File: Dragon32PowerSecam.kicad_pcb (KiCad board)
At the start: 2 copper layers, 246 x 83.9 mm, 24 parts, among them IC1 MC3346, IC2 MC3346, IC3 MC3346

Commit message: video tracing
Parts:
- added R10: 220R, Dragon:R_Axial_DIN0309_L9.0mm_D2.5mm_P12.70mm_Horizontal, F.Cu at (82.4, 50.8)
- added R12: 220R, Dragon:R_Axial_DIN0309_L9.0mm_D2.5mm_P12.70mm_Horizontal, F.Cu at (82.4, 55.9)
- added R14: 220R, Dragon:R_Axial_DIN0309_L9.0mm_D2.5mm_P12.70mm_Horizontal, F.Cu at (82.4, 48.3)
- added R40: 500R, Dragon:R_Axial_DIN0309_L9.0mm_D2.5mm_P12.70mm_Horizontal, F.Cu at (67.4, 60.9)
- added R47: 2R2, Dragon:R_Axial_DIN0309_L9.0mm_D2.5mm_P12.70mm_Horizontal, F.Cu at (58.0, 34.5)
- added R48: 2R2, Dragon:R_Axial_DIN0309_L9.0mm_D2.5mm_P12.70mm_Horizontal, F.Cu at (58.0, 32.0)
- added R8: 220R, Dragon:R_Axial_DIN0309_L9.0mm_D2.5mm_P12.70mm_Horizontal, F.Cu at (82.4, 53.4)
- added T1: Q_NPN_CBE, Package_TO_SOT_THT:TO-92, F.Cu at (94.8, 61.3)
- added T2: Q_NPN_CBE, Package_TO_SOT_THT:TO-92, F.Cu at (99.6, 61.3)
- added T3: Q_NPN_CBE, Package_TO_SOT_THT:TO-92, F.Cu at (90.1, 61.3)
- added T4: Q_NPN_CBE, Package_TO_SOT_THT:TO-92, F.Cu at (104.3, 61.3)
- added UM1: ~, Dragon:RF_Modulator_Astec_UM1601, F.Cu at (46.9, 71.9)
- moved C13 4.66 mm to (54.2, 29.4)
- moved R36 2.35 mm to (58.0, 29.5)
- moved C14 2.19 mm to (78.2, 53.5)
- moved C19 2.17 mm to (68.9, 42.4)
- moved C16 1.99 mm to (67.4, 79.8)
- moved IC2 1.79 mm to (84.9, 64.4)
- moved IC3 1.70 mm to (69.9, 64.4)
- moved C17 1.70 mm to (69.9, 83.2)
- moved C15 1.70 mm to (80.0, 72.0)
- moved L1 1.10 mm to (71.1, 52.2)
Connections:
- C14 pad 1: unconnected-(C14-Pad1) -> /Video/ic3_11
- C14 pad 2: unconnected-(C14-Pad2) -> /Video/ic3_8
- C15 pad 2: unconnected-(C15-Pad2) -> /Video/ic3_11
- C17 pad 1: unconnected-(C17-Pad1) -> /Video/ic3_4
- C19 pad 1: unconnected-(C19-Pad1) -> /Video/ic3_4
- C19 pad 2: unconnected-(C19-Pad2) -> Net-(C19-Pad2)
- IC3 pad 11: unconnected-(IC3-Pad11) -> /Video/ic3_11
- IC3 pad 14: unconnected-(IC3-Pad14) -> Net-(IC3-Pad14)
- IC3 pad 2: unconnected-(IC3-Pad2) -> Net-(IC3-Pad2)
- IC3 pad 3: unconnected-(IC3-Pad3) -> Net-(IC3-Pad14)
- IC3 pad 4: unconnected-(IC3-Pad4) -> /Video/ic3_4
- IC3 pad 5: unconnected-(IC3-Pad5) -> /Video/ic3_5
- IC3 pad 8: unconnected-(IC3-Pad8) -> /Video/ic3_8
- IC3 pad 9: unconnected-(IC3-Pad9) -> Net-(IC3-Pad2)
- L1 pad 1: unconnected-(L1-Pad1) -> /Video/ic3_8
- L1 pad 3: unconnected-(L1-Pad3) -> /Video/ic3_11
- L1 pad 5: unconnected-(L1-GND-Pad5) -> GND
- PL11 pad 4: unconnected-(PL11-Pad4) -> pl11_4
- PL11 pad 5: unconnected-(PL11-Pad5) -> pl11_5
- PL11 pad 6: unconnected-(PL11-Pad6) -> pl11_6
- PL11 pad 7: unconnected-(PL11-Pad7) -> pl11_7
- R39 pad 2: unconnected-(R39-Pad2) -> Net-(UM1-Bias)
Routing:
- net GND: track 4.93 -> 94.8 mm, vias 0 -> 4
- net /Video/ic3_5: track 0.00 -> 74.6 mm
- net /Video/ic3_4: track 0.00 -> 54.9 mm
- net /Video/ic3_8: track 0.00 -> 53.1 mm
- net unconnected-(IC3-Pad13): track 0.00 -> 36.2 mm
- net unconnected-(IC3-Pad12): track 0.00 -> 31.5 mm
- net Net-(IC3-Pad2): track 0.00 -> 28.1 mm
- net /Video/ic3_11: track 0.00 -> 26.1 mm, vias 0 -> 1
- net unconnected-(R48-Pad2): track 0.00 -> 23.8 mm
- net pl11_7: track 0.00 -> 16.5 mm
- net pl11_4: track 0.00 -> 13.8 mm
- net Net-(C19-Pad2): track 0.00 -> 13.1 mm
- net Net-(IC3-Pad14): track 0.00 -> 9.72 mm
- net pl11_6: track 0.00 -> 9.39 mm
- net pl11_5: track 0.00 -> 9.36 mm
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
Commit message: more video tracing
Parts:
- added C1: 1M250, Capacitor_THT:C_Rect_L16.5mm_W5.0mm_P15.00mm_MKT, F.Cu at (121.3, 97.3)
- added C2: 100nF, Capacitor_THT:C_Disc_D4.3mm_W1.9mm_P5.00mm, F.Cu at (123.1, 78.1)
- added D9: 1N, Diode_THT:D_A-405_P12.70mm_Horizontal, F.Cu at (117.7, 94.8)
- added R11: 220R, Dragon:R_Axial_DIN0309_L9.0mm_D2.5mm_P12.70mm_Horizontal, F.Cu at (97.2, 72.0)
- added R13: 220R, Dragon:R_Axial_DIN0309_L9.0mm_D2.5mm_P12.70mm_Horizontal, F.Cu at (97.2, 64.4)
- added R15: 220R, Dragon:R_Axial_DIN0309_L9.0mm_D2.5mm_P12.70mm_Horizontal, F.Cu at (97.2, 74.5)
- added R16: 220R, Dragon:R_Axial_DIN0309_L9.0mm_D2.5mm_P12.70mm_Horizontal, F.Cu at (82.5, 85.9)
- added R17: 220R, Dragon:R_Axial_DIN0309_L9.0mm_D2.5mm_P12.70mm_Horizontal, F.Cu at (112.2, 94.7)
- added R18: 220R, Resistor_THT:R_Axial_DIN0207_L6.3mm_D2.5mm_P10.16mm_Horizontal, F.Cu at (117.2, 79.6)
- added R19: 220R, Dragon:R_Axial_DIN0309_L9.0mm_D2.5mm_P12.70mm_Horizontal, F.Cu at (109.7, 94.7)
- added R20: 220R, Resistor_THT:R_Axial_DIN0207_L6.3mm_D2.5mm_P10.16mm_Horizontal, F.Cu at (119.7, 79.6)
- added R21: 220R, Dragon:R_Axial_DIN0309_L9.0mm_D2.5mm_P12.70mm_Horizontal, F.Cu at (114.8, 94.7)
- added R22: 220R, Dragon:R_Axial_DIN0309_L9.0mm_D2.5mm_P12.70mm_Horizontal, F.Cu at (94.9, 66.9)
- added R23: 220R, Dragon:R_Axial_DIN0309_L9.0mm_D2.5mm_P12.70mm_Horizontal, F.Cu at (97.7, 51.9)
- added R24: 220R, Dragon:R_Axial_DIN0309_L9.0mm_D2.5mm_P12.70mm_Horizontal, F.Cu at (82.5, 88.5)
- added R25: 220R, Dragon:R_Axial_DIN0309_L9.0mm_D2.5mm_P12.70mm_Horizontal, F.Cu at (97.7, 46.9)
- added R26: 220R, Dragon:R_Axial_DIN0309_L9.0mm_D2.5mm_P12.70mm_Horizontal, F.Cu at (82.5, 91.0)
- added R27: 220R, Dragon:R_Axial_DIN0309_L9.0mm_D2.5mm_P12.70mm_Horizontal, F.Cu at (97.7, 49.4)
- added R28: 220R, Dragon:R_Axial_DIN0309_L9.0mm_D2.5mm_P12.70mm_Horizontal, F.Cu at (97.7, 54.5)
- added R29: 220R, Dragon:R_Axial_DIN0309_L9.0mm_D2.5mm_P12.70mm_Horizontal, F.Cu at (82.5, 96.1)
- added R30: 220R, Dragon:R_Axial_DIN0309_L9.0mm_D2.5mm_P12.70mm_Horizontal, F.Cu at (82.5, 93.5)
- added R31: 220R, Dragon:R_Axial_DIN0309_L9.0mm_D2.5mm_P12.70mm_Horizontal, F.Cu at (82.5, 101.2)
- added R32: 220R, Dragon:R_Axial_DIN0309_L9.0mm_D2.5mm_P12.70mm_Horizontal, F.Cu at (82.5, 98.6)
- added R33: 220R, Dragon:R_Axial_DIN0309_L9.0mm_D2.5mm_P12.70mm_Horizontal, F.Cu at (97.3, 96.1)
- added R34: 220R, Dragon:R_Axial_DIN0309_L9.0mm_D2.5mm_P12.70mm_Horizontal, F.Cu at (97.2, 79.6)
- added R35: 220R, Dragon:R_Axial_DIN0309_L9.0mm_D2.5mm_P12.70mm_Horizontal, F.Cu at (84.5, 103.7)
- added R37: 220R, Dragon:R_Axial_DIN0309_L9.0mm_D2.5mm_P12.70mm_Horizontal, F.Cu at (97.7, 41.8)
- added R38: 220R, Dragon:R_Axial_DIN0309_L9.0mm_D2.5mm_P12.70mm_Horizontal, F.Cu at (97.7, 39.2)
- added R41: 220R, Dragon:R_Axial_DIN0309_L9.0mm_D2.5mm_P12.70mm_Horizontal, F.Cu at (67.7, 88.5)
- added R42: 220R, Dragon:R_Axial_DIN0309_L9.0mm_D2.5mm_P12.70mm_Horizontal, F.Cu at (67.7, 91.0)
- added R43: 220R, Dragon:R_Axial_DIN0309_L9.0mm_D2.5mm_P12.70mm_Horizontal, F.Cu at (67.7, 96.1)
- added R44: 220R, Dragon:R_Axial_DIN0309_L9.0mm_D2.5mm_P12.70mm_Horizontal, F.Cu at (67.7, 93.5)
- added R45: 220R, Dragon:R_Axial_DIN0309_L9.0mm_D2.5mm_P12.70mm_Horizontal, F.Cu at (67.7, 85.9)
- added R46: 220R, Dragon:R_Axial_DIN0309_L9.0mm_D2.5mm_P12.70mm_Horizontal, F.Cu at (67.7, 98.6)
- added R49: 220R, Dragon:R_Axial_DIN0309_L9.0mm_D2.5mm_P12.70mm_Horizontal, F.Cu at (97.7, 44.3)
- added R50: 220R, Dragon:R_Axial_DIN0309_L9.0mm_D2.5mm_P12.70mm_Horizontal, F.Cu at (97.7, 36.7)
- added R6: 220R, Dragon:R_Axial_DIN0309_L9.0mm_D2.5mm_P12.70mm_Horizontal, F.Cu at (97.2, 77.1)
- added R7: 220R, Dragon:R_Axial_DIN0309_L9.0mm_D2.5mm_P12.70mm_Horizontal, F.Cu at (97.2, 69.5)
- added R9: 220R, Dragon:R_Axial_DIN0309_L9.0mm_D2.5mm_P12.70mm_Horizontal, F.Cu at (97.2, 66.9)
- C11: footprint Capacitor_THT:C_Disc_D4.3mm_W1.9mm_P5.00mm -> Capacitor_THT:C_Disc_D3.0mm_W2.0mm_P2.50mm
- PL9: value DE9_Plug_MountingHoles -> External Power
- T1, T2, T3, T4: footprint Package_TO_SOT_THT:TO-92 -> Package_TO_SOT_THT:TO-92_Wide
- moved C18 3.89 mm to (67.7, 101.1)
- moved C12 2.42 mm to (113.7, 74.6)
- moved C11 2.39 mm to (114.3, 79.6)
- moved T4 2.02 mm to (106.3, 61.8)
- moved IC1 2.00 mm to (99.4, 83.4)
- moved R10 1.42 mm to (82.5, 49.4)
- moved R12 1.42 mm to (82.5, 54.5)
- moved R14 1.42 mm to (82.5, 46.9)
- moved R8 1.42 mm to (82.5, 51.9)
- moved T2 1.25 mm to (100.7, 61.8)
- moved C10 0.77 mm to (109.8, 97.4)
- moved T3 0.70 mm to (89.6, 61.8)
- moved T1 0.61 mm to (95.1, 61.8)
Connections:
- C10 pad 2: unconnected-(C10-Pad2) -> GND
- C15 pad 1: unconnected-(C15-Pad1) -> Net-(C15-Pad1)
- C16 pad 1: unconnected-(C16-Pad1) -> Net-(C16-Pad1)
- C16 pad 2: unconnected-(C16-Pad2) -> Net-(C16-Pad2)
- C17 pad 2: unconnected-(C17-Pad2) -> /Video/ic3_2
- C18 pad 1: unconnected-(C18-Pad1) -> GND
- C18 pad 2: unconnected-(C18-Pad2) -> Net-(C18-Pad2)
- IC1 pad 1: unconnected-(IC1-Pad1) -> /Video/ic1_1
- IC1 pad 10: unconnected-(IC1-Pad10) -> /Video/ic1_10
- IC1 pad 12: unconnected-(IC1-Pad12) -> /Video/ic1_12
- IC1 pad 13: unconnected-(IC1-Pad13) -> /Video/ic1_13
- IC1 pad 14: unconnected-(IC1-Pad14) -> /Video/ic1_14
- IC1 pad 7: unconnected-(IC1-Pad7) -> /Video/ic1_7
- IC1 pad 8: unconnected-(IC1-Pad8) -> +5V
- IC2 pad 1: unconnected-(IC2-Pad1) -> /Video/ic2_1
- IC2 pad 10: unconnected-(IC2-Pad10) -> /Video/ic2_10
- IC2 pad 11: unconnected-(IC2-Pad11) -> /Video/ic2_11
- IC2 pad 12: unconnected-(IC2-Pad12) -> /Video/ic2_12
- IC2 pad 13: unconnected-(IC2-Pad13) -> /Video/ic2_13
- IC2 pad 14: unconnected-(IC2-Pad14) -> +5V
- IC2 pad 2: unconnected-(IC2-Pad2) -> /Video/ic2_6
- IC2 pad 3: unconnected-(IC2-Pad3) -> /Video/ic1_14
- IC2 pad 4: unconnected-(IC2-Pad4) -> /Video/ic2_6
- IC2 pad 5: unconnected-(IC2-Pad5) -> /Video/ic2_5
- IC2 pad 6: unconnected-(IC2-Pad6) -> /Video/ic2_6
- IC2 pad 7: unconnected-(IC2-Pad7) -> /Video/ic2_7
- IC2 pad 8: unconnected-(IC2-Pad8) -> /Video/ic2_8
- IC2 pad 9: unconnected-(IC2-Pad9) -> /Video/ic2_6
- IC3 pad 1: unconnected-(IC3-Pad1) -> /Video/ic3_8
- IC3 pad 10: unconnected-(IC3-Pad10) -> Net-(IC3-Pad10)
- IC3 pad 12: unconnected-(IC3-Pad12) -> Net-(C16-Pad2)
- IC3 pad 13: unconnected-(IC3-Pad13) -> Net-(IC3-Pad13)
- IC3 pad 2: Net-(IC3-Pad2) -> /Video/ic3_2
- IC3 pad 6: unconnected-(IC3-Pad6) -> Net-(C16-Pad1)
- IC3 pad 7: unconnected-(IC3-Pad7) -> Net-(IC3-Pad10)
- IC3 pad 9: Net-(IC3-Pad2) -> /Video/ic3_2
- PL11 pad 1: unconnected-(PL11-Pad1) -> pl11_1
- PL11 pad 2: unconnected-(PL11-Pad2) -> pl11_2
- PL11 pad 3: unconnected-(PL11-Pad3) -> pl11_3
- PL9 pad 1: unconnected-(PL9-Pad1) -> /Power/pl9_1
- PL9 pad 2: unconnected-(PL9-Pad2) -> /Power/pl9_2
- PL9 pad 3: unconnected-(PL9-Pad3) -> /Power/pl9_3
- PL9 pad 4: unconnected-(PL9-Pad4) -> GND
- PL9 pad 5: unconnected-(PL9-Pad5) -> /Power/pl9_5
- PL9 pad 6: unconnected-(PL9-Pad6) -> /Power/pl9_1
- PL9 pad 7: unconnected-(PL9-Pad7) -> /Power/pl9_2
- PL9 pad 8: unconnected-(PL9-Pad8) -> GND
- PL9 pad 9: unconnected-(PL9-Pad9) -> GND
- R10 pad 2: unconnected-(R10-Pad2) -> Net-(T2-E)
- R12 pad 2: unconnected-(R12-Pad2) -> Net-(T1-E)
- R14 pad 2: unconnected-(R14-Pad2) -> Net-(T4-E)
- R36 pad 2: unconnected-(R36-Pad2) -> +5V
- R40 pad 1: unconnected-(R40-Pad1) -> /Video/ic3_2
- R48 pad 2: unconnected-(R48-Pad2) -> SOUND
- R8 pad 2: unconnected-(R8-Pad2) -> Net-(T3-E)
- SW1 pad 11: unconnected-(SW1-B-Pad11) -> /Power/pl9_5
- SW1 pad 2: unconnected-(SW1-B-Pad2) -> /Power/pl9_1
- SW1 pad 5: (no net) -> /Power/pl9_2
- SW1 pad 8: unconnected-(SW1-B-Pad8) -> /Power/pl9_3
- T1 pad 1: unconnected-(T1-C-Pad1) -> +5V
- T1 pad 2: unconnected-(T1-B-Pad2) -> /Video/ic2_5
- T1 pad 3: unconnected-(T1-E-Pad3) -> Net-(T1-E)
- T2 pad 1: unconnected-(T2-C-Pad1) -> +5V
- T2 pad 2: unconnected-(T2-B-Pad2) -> /Video/ic2_11
- T2 pad 3: unconnected-(T2-E-Pad3) -> Net-(T2-E)
- T3 pad 1: unconnected-(T3-C-Pad1) -> +5V
- T3 pad 2: unconnected-(T3-B-Pad2) -> /Video/ic2_1
- T3 pad 3: unconnected-(T3-E-Pad3) -> Net-(T3-E)
- T4 pad 1: unconnected-(T4-C-Pad1) -> +5V
- T4 pad 2: unconnected-(T4-B-Pad2) -> /Video/ic2_8
- T4 pad 3: unconnected-(T4-E-Pad3) -> Net-(T4-E)
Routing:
- net +5V: track 0.00 -> 225.2 mm, vias 0 -> 1
- net SOUND: track 0.00 -> 114.4 mm, vias 0 -> 1
- net -5V: track 0.00 -> 108.1 mm
- net +12V: track 0.00 -> 89.1 mm
- net /Power/pl9_2: track 0.00 -> 57.3 mm
- net /Video/ic1_14: track 0.00 -> 56.3 mm, vias 0 -> 1
- net /Video/ic2_6: track 0.00 -> 55.7 mm
- net Net-(C16-Pad2): track 0.00 -> 55.0 mm
- net /Video/ic1_12: track 0.00 -> 53.0 mm
- net /Power/pl9_3: track 0.00 -> 52.9 mm
- net /Video/ic3_2: track 0.00 -> 52.0 mm
- net /Video/ic2_13: track 0.00 -> 45.0 mm
- net /Power/pl9_5: track 0.00 -> 40.8 mm
- net Net-(IC3-Pad13): track 0.00 -> 38.1 mm
- net /Power/pl9_1: track 0.00 -> 38.0 mm
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
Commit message: power tracing
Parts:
- added C5: 220uF 35V, Capacitor_THT:CP_Axial_L25.0mm_D10.0mm_P30.00mm_Horizontal, F.Cu at (150.0, 50.5)
- added C6: 4700uF 16V, Capacitor_THT:CP_Axial_L34.5mm_D20.0mm_P41.00mm_Horizontal, F.Cu at (211.3, 38.1)
- added C9: 4700uF 16V, Capacitor_THT:CP_Axial_L34.5mm_D20.0mm_P41.00mm_Horizontal, F.Cu at (218.5, 38.2)
- added D1: 1N5401, Diode_THT:D_DO-201AD_P15.24mm_Horizontal, F.Cu at (127.4, 50.7)
- added D2: 1N5401, Diode_THT:D_DO-201AD_P15.24mm_Horizontal, F.Cu at (127.4, 56.4)
- added D3: 1N4002, Diode_THT:D_DO-41_SOD81_P10.16mm_Horizontal, F.Cu at (133.0, 60.9)
- added D4: 1N4002, Diode_THT:D_DO-41_SOD81_P10.16mm_Horizontal, F.Cu at (133.0, 64.4)
- added D5: 1N5401, Diode_THT:D_DO-201AD_P15.24mm_Horizontal, F.Cu at (127.4, 68.9)
- added D6: 1N5401, Diode_THT:D_DO-201AD_P15.24mm_Horizontal, F.Cu at (127.5, 74.6)
- added D7: 1N4002, Diode_THT:D_DO-41_SOD81_P10.16mm_Horizontal, F.Cu at (133.0, 79.0)
- added D8: 1N4002, Diode_THT:D_DO-41_SOD81_P10.16mm_Horizontal, F.Cu at (133.0, 82.2)
- added R2: 220R, Dragon:R_Axial_DIN0309_L9.0mm_D2.5mm_P12.70mm_Horizontal, F.Cu at (125.3, 94.7)
- added R5: 180R, Resistor_THT:R_Axial_DIN0516_L15.5mm_D5.0mm_P20.32mm_Horizontal, F.Cu at (158.1, 75.0)
- added REG1: LM309K, Package_TO_SOT_THT:TO-3, F.Cu at (184.5, 68.5)
- moved C11 0.86 mm to (113.5, 79.6)
- moved C2 0.58 mm to (122.5, 78.1)
- moved C12 0.36 mm to (113.4, 74.6)
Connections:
- C1 pad 2: unconnected-(C1-Pad2) -> -5V
- C10 pad 1: unconnected-(C10-Pad1) -> LUMA
- C11 pad 1: unconnected-(C11-Pad1) -> Net-(C11-Pad1)
- C11 pad 2: unconnected-(C11-Pad2) -> /Video/ic1_3
- C12 pad 1: unconnected-(C12-Pad1) -> /Video/ic1_1
- C12 pad 2: unconnected-(C12-Pad2) -> /Video/ic2_12
- C2 pad 1: unconnected-(C2-Pad1) -> GND
- D9 pad 1: unconnected-(D9-K-Pad1) -> /Video/ic2_12
- D9 pad 2: unconnected-(D9-A-Pad2) -> Net-(D9-A)
- IC1 pad 11: unconnected-(IC1-Pad11) -> +5V
- IC1 pad 3: unconnected-(IC1-Pad3) -> /Video/ic1_3
- IC2 pad 2: /Video/ic2_6 -> GND
- IC2 pad 4: /Video/ic2_6 -> GND
- IC2 pad 6: /Video/ic2_6 -> GND
- IC2 pad 9: /Video/ic2_6 -> GND
- R17 pad 1: unconnected-(R17-Pad1) -> GND
- R17 pad 2: unconnected-(R17-Pad2) -> Net-(C11-Pad1)
- R18 pad 1: unconnected-(R18-Pad1) -> /Video/ic1_3
- R19 pad 1: unconnected-(R19-Pad1) -> GND
- R19 pad 2: unconnected-(R19-Pad2) -> /Video/ic1_3
- R20 pad 1: unconnected-(R20-Pad1) -> Net-(D9-A)
- R21 pad 1: unconnected-(R21-Pad1) -> GND
- R21 pad 2: unconnected-(R21-Pad2) -> Net-(D9-A)
- R35 pad 2: /Video/ic2_6 -> GND
- SW1 pad 10: unconnected-(SW1-A-Pad10) -> Net-(D4-K)
- SW1 pad 3: unconnected-(SW1-C-Pad3) -> Net-(D1-K)
- SW1 pad 6: unconnected-(SW1-C-Pad6) -> Net-(D2-K)
- SW1 pad 7: unconnected-(SW1-A-Pad7) -> Net-(D3-K)
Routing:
- net -5V: track 108.1 -> 280.6 mm
- net Net-(D7-K): track 0.00 -> 151.9 mm
- net /Power/VI: track 0.00 -> 127.6 mm
- net GND: track 123.8 -> 218.6 mm, vias 5 -> 6
- net +5V: track 225.2 -> 293.5 mm
- net /Video/ic2_6: track 55.7 -> 0.00 mm
- net Net-(D4-K): track 0.00 -> 53.6 mm, vias 0 -> 1
- net Net-(D3-K): track 0.00 -> 42.9 mm
- net Net-(D3-A): track 0.00 -> 42.4 mm
- net /Video/ic2_12: track 34.5 -> 75.5 mm, vias 1 -> 2
- net Net-(D2-K): track 0.00 -> 38.0 mm
- net Net-(D1-K): track 0.00 -> 33.7 mm
- net /Video/ic1_3: track 0.00 -> 26.4 mm
- net unconnected-(SW1-A-Pad7): track 19.4 -> 0.00 mm
- net unconnected-(SW1-C-Pad6): track 10.1 -> 0.00 mm
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- added copper zone on B.Cu, net /Power/VI

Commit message: layout and routing complete
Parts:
- added C3: 1M250, Capacitor_THT:C_Rect_L16.5mm_W5.0mm_P15.00mm_MKT, F.Cu at (146.7, 107.8)
- added C4: 1M250, Capacitor_THT:C_Rect_L16.5mm_W5.0mm_P15.00mm_MKT, F.Cu at (157.3, 107.7)
- added C7: 10nF, Capacitor_THT:C_Disc_D4.7mm_W2.5mm_P5.00mm, F.Cu at (257.7, 51.6)
- added C8: 470uF 50V, Capacitor_THT:CP_Axial_L30.0mm_D10.0mm_P35.00mm_Horizontal, F.Cu at (267.6, 86.7)
- added R3: 220R, Dragon:R_Axial_DIN0309_L9.0mm_D2.5mm_P12.70mm_Horizontal, F.Cu at (150.7, 92.8)
- added R4: 220R, Dragon:R_Axial_DIN0309_L9.0mm_D2.5mm_P12.70mm_Horizontal, F.Cu at (153.3, 92.8)
- added REG2: L7905, Package_TO_SOT_THT:TO-220-3_Vertical, F.Cu at (257.2, 67.7)
- added REG3: LM7812_TO220, Package_TO_SOT_THT:TO-220-3_Vertical, F.Cu at (257.2, 88.6)
- C12, C19: value C_Polarized_Small -> 1uF 25V Tant
- C13: value C_Polarized_Small -> 1uF 25V
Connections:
- C13 pad 1: Net-(UM1-Audio) -> /Video/ic3_8
- C13 pad 2: unconnected-(C13-Pad2) -> GND
- C2 pad 2: unconnected-(C2-Pad2) -> /Power/VI
- R2 pad 1: unconnected-(R2-Pad1) -> GND
- R36 pad 1: Net-(UM1-Audio) -> /Video/ic3_8
- R5 pad 1: unconnected-(R5-Pad1) -> Net-(REG2-VI)
- UM1 pad 3: Net-(UM1-Audio) -> /Video/ic3_8
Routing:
- net +12V: track 89.1 -> 251.3 mm
- net Net-(REG2-VI): track 0.00 -> 127.8 mm
- net /Video/ic3_8: track 64.8 -> 96.3 mm
- net Net-(UM1-Audio): track 16.7 -> 0.00 mm
- net GND: track 218.6 -> 234.6 mm
- net -5V: track 280.6 -> 271.7 mm
- net Net-(D7-K): track 151.9 -> 157.6 mm
- net /Power/VI: track 127.6 -> 131.6 mm
- net /Power/pl9_2: track 57.0 -> 56.5 mm

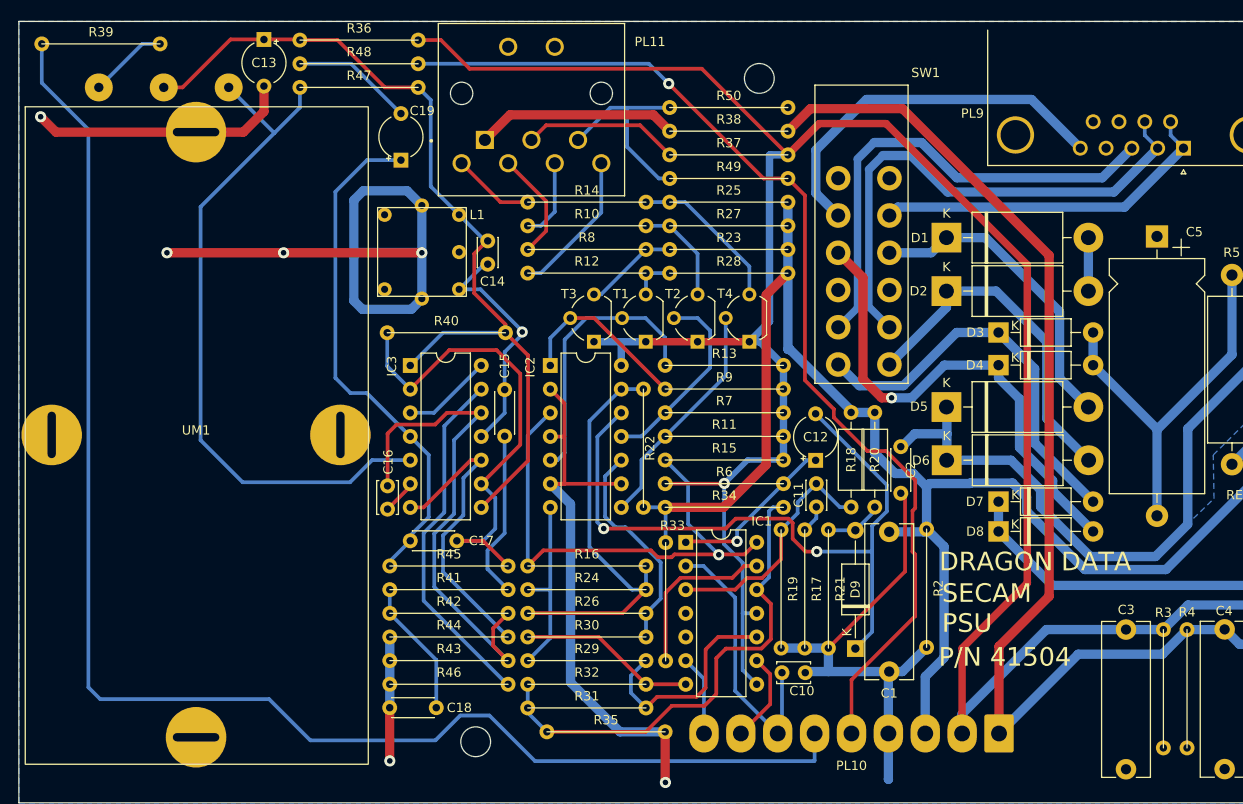
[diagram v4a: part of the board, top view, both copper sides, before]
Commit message: rationalise rgb circuit
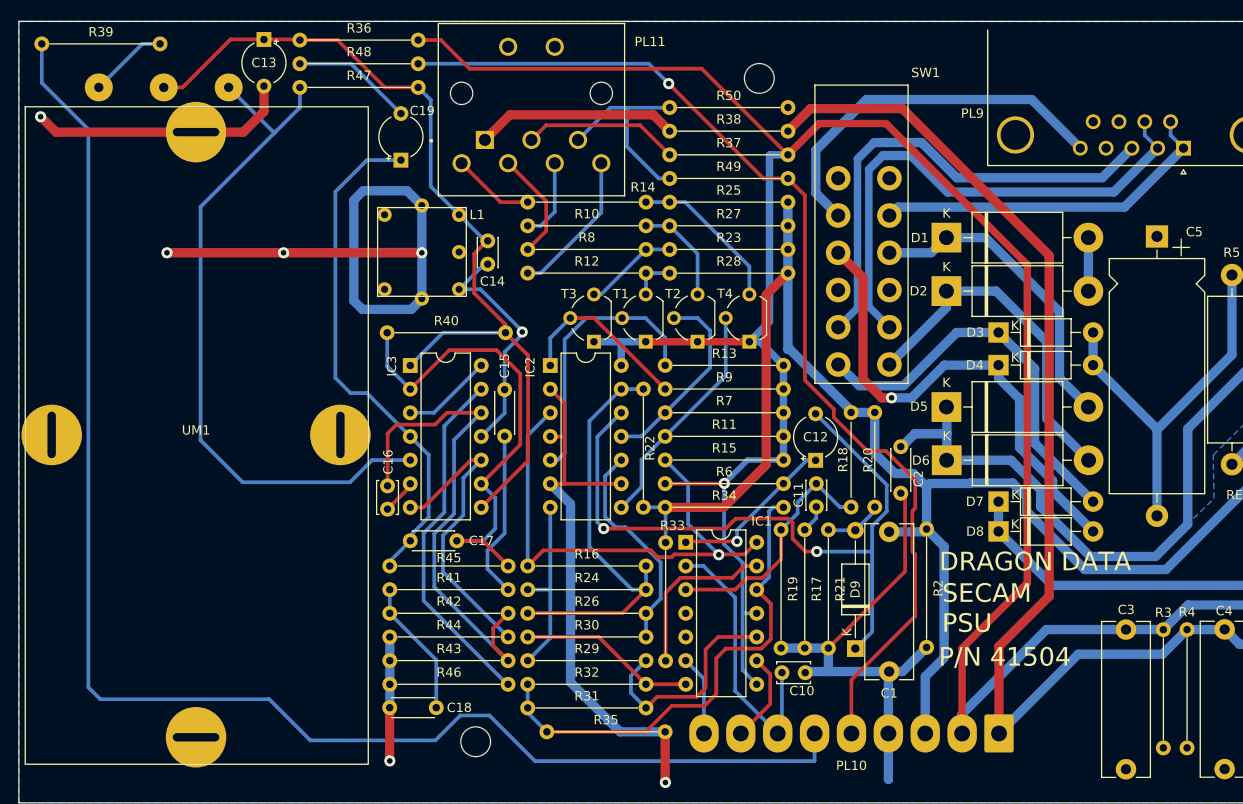
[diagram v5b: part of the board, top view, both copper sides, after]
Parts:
- IC1, IC2, IC3: value MC3346 -> CA3046
- R10, R12, R14, R8: value 220R -> 22R
- R11, R13, R7, R9: value 220R -> 3K9
- R15, R24, R26: value 220R -> 1K
- R16: value 220R -> 470R
- R18: value 220R -> 1k2; footprint Resistor_THT:R_Axial_DIN0207_L6.3mm_D2.5mm_P10.16mm_Horizontal -> Dragon:R_Axial_DIN0207_L6.3mm_D2.5mm_P10.16mm_Horizontal
- R19, R38: value 220R -> 820R
- R2, R23, R25, R27, R28, R3, R4, R49: value 220R -> 10K
- R20: value 220R -> 1K2; footprint Resistor_THT:R_Axial_DIN0207_L6.3mm_D2.5mm_P10.16mm_Horizontal -> Dragon:R_Axial_DIN0207_L6.3mm_D2.5mm_P10.16mm_Horizontal
- R29, R30, R44: value 220R -> 2K2
- R31: value 220R -> 33K
- R32: value 220R -> 120K
- R33: value 220R -> 330R
- R34: value 220R -> 12K
- R35: value 220R -> 56K
- R37: value 220R -> 390R
- R40: value 500R -> 470R
- R41: value 220R -> 6K8
- R43, R46: value 220R -> 270R
- R47: value 2R2 -> 3K9
- R48: value 2R2 -> 12K
- R50: value 220R -> 27K
- R6: value 220R -> 560R
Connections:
- net /Video/ic1_1 renamed Net-(C12-Pad1)
- net /Video/ic1_10 renamed /Video/R-Y
- net /Video/ic1_12 renamed Net-(IC1-Pad12)
- net /Video/ic1_13 renamed Net-(IC1-Pad13)
- net /Video/ic1_14 renamed /Video/G-Y
- net /Video/ic1_3 renamed Net-(C11-Pad2)
- net /Video/ic1_7 renamed /Video/B-Y
- net /Video/ic2_1 renamed /Video/(G-Y)+Y
- net /Video/ic2_10 renamed Net-(IC2-Pad10)
- net /Video/ic2_11 renamed /Video/(B-Y)+Y
- net /Video/ic2_12 renamed /Video/homogenised_luma
- net /Video/ic2_13 renamed /Video/Y
- net /Video/ic2_5 renamed /Video/GSync
- net /Video/ic2_7 renamed Net-(IC2-Pad7)
- net /Video/ic2_8 renamed /Video/(R-Y)+Y

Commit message: update labelling
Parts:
- added TP1: TestPoint, TestPoint:TestPoint_THTPad_D1.0mm_Drill0.5mm, F.Cu at (82.1, 60.9)
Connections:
- net U11 renamed SECAM_COMP
- C1 pad 1: GND -> pl11_3
- C10 pad 2: GND -> pl11_3
- C13 pad 2: GND -> pl11_3
- C18 pad 1: GND -> pl11_3
- C2 pad 1: GND -> pl11_3
- C3 pad 1: GND -> pl11_3
- C4 pad 1: GND -> pl11_3
- C5 pad 1: GND -> pl11_3
- C6 pad 2: GND -> pl11_3
- C7 pad 1: GND -> pl11_3
- C8 pad 2: GND -> pl11_3
- C9 pad 2: GND -> pl11_3
- D1 pad 2: GND -> pl11_3
- D2 pad 2: GND -> pl11_3
- IC2 pad 2: GND -> pl11_3
- IC2 pad 4: GND -> pl11_3
- IC2 pad 6: GND -> pl11_3
- IC2 pad 9: GND -> pl11_3
- L1 pad 5: GND -> pl11_3
- PL10 pad 4: GND -> pl11_3
- PL9 pad 4: GND -> pl11_3
- PL9 pad 8: GND -> pl11_3
- PL9 pad 9: GND -> pl11_3
- R17 pad 1: GND -> pl11_3
- R19 pad 1: GND -> pl11_3
- R2 pad 1: GND -> pl11_3
- R21 pad 1: GND -> pl11_3
- R3 pad 2: GND -> pl11_3
- R35 pad 2: GND -> pl11_3
- R4 pad 2: GND -> pl11_3
- R43 pad 1: GND -> pl11_3
- R44 pad 1: GND -> pl11_3
- R46 pad 1: GND -> pl11_3
- R50 pad 2: GND -> pl11_3
- REG1 pad 3: GND -> pl11_3
- REG2 pad 1: GND -> pl11_3
- REG3 pad 2: GND -> pl11_3
- UM1 pad 4: GND -> pl11_3
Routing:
- net GND: track 234.6 -> 0.00 mm, vias 6 -> 0
- net pl11_3: track 21.5 -> 256.1 mm, vias 0 -> 6
- net /Video/ic3_11: track 26.1 -> 26.4 mm, vias 1 -> 0
- added copper zone on B.Cu, net pl11_3
- removed copper zone on B.Cu, net GND
